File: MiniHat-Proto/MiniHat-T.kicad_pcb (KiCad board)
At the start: 2 copper layers, 19.5 x 16 mm, 1 part, among them J101 Interface

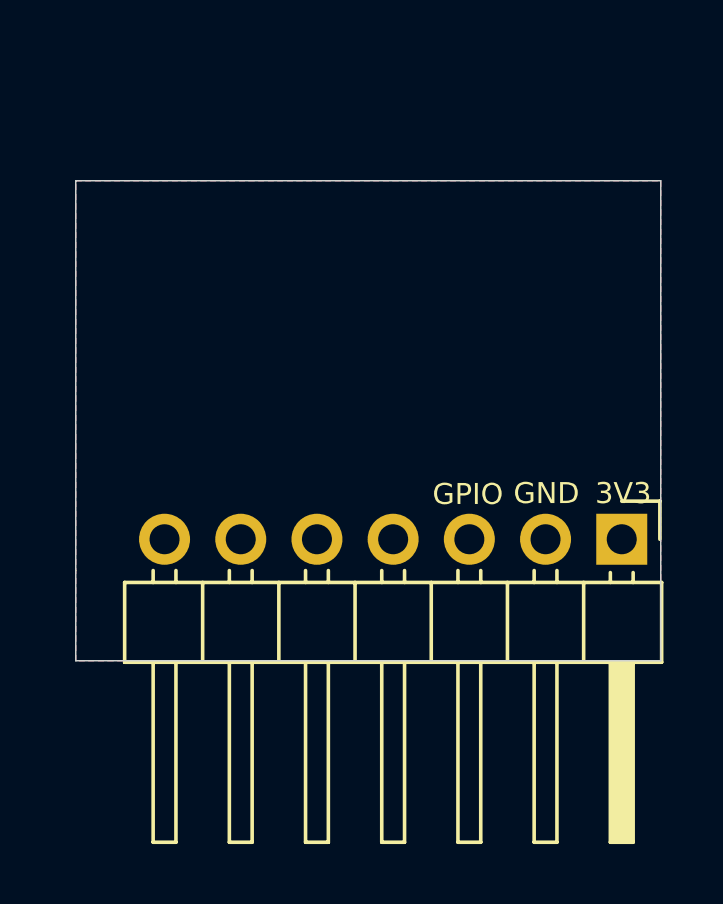
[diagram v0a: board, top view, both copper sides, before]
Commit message: Standardize on 20mm x 20mm boards with 7pin header
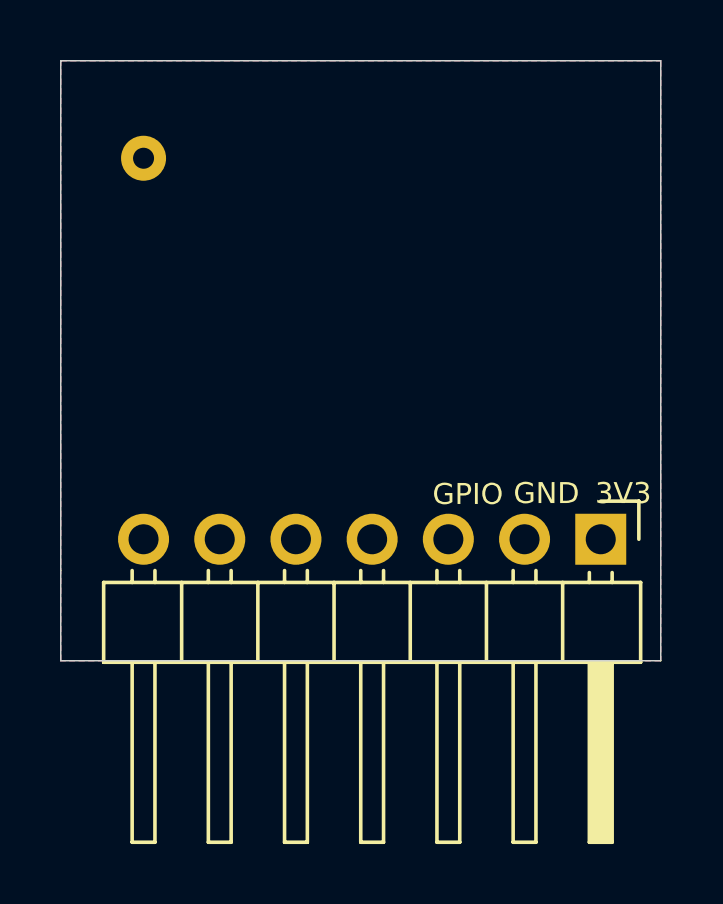
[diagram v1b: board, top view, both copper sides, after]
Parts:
- added REF**: TestPoint_THTPad_D1.5mm_Drill0.7mm, TestPoint:TestPoint_THTPad_D1.5mm_Drill0.7mm, F.Cu at (122.8, 76.2)
- moved J101 0.70 mm to (138.0, 89.0)
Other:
- board size 19.5 x 16 mm -> 20 x 20 mm
- board text added: "Hole here is for Single pin to support board edge if needed for connectors when Horizontal on SH-ESP32"
- board text added: "If extending board raise bottom edge 5mm to clear components on SH-ESP32"
- board text removed: "Leave Free if extending board raise bottom edge 4mm to clear components on SH-ESP32"
